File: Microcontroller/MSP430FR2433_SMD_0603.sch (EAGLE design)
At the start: 7 parts, among them IC1 MSP430FR2433IRGET, Y1 32.768kHz

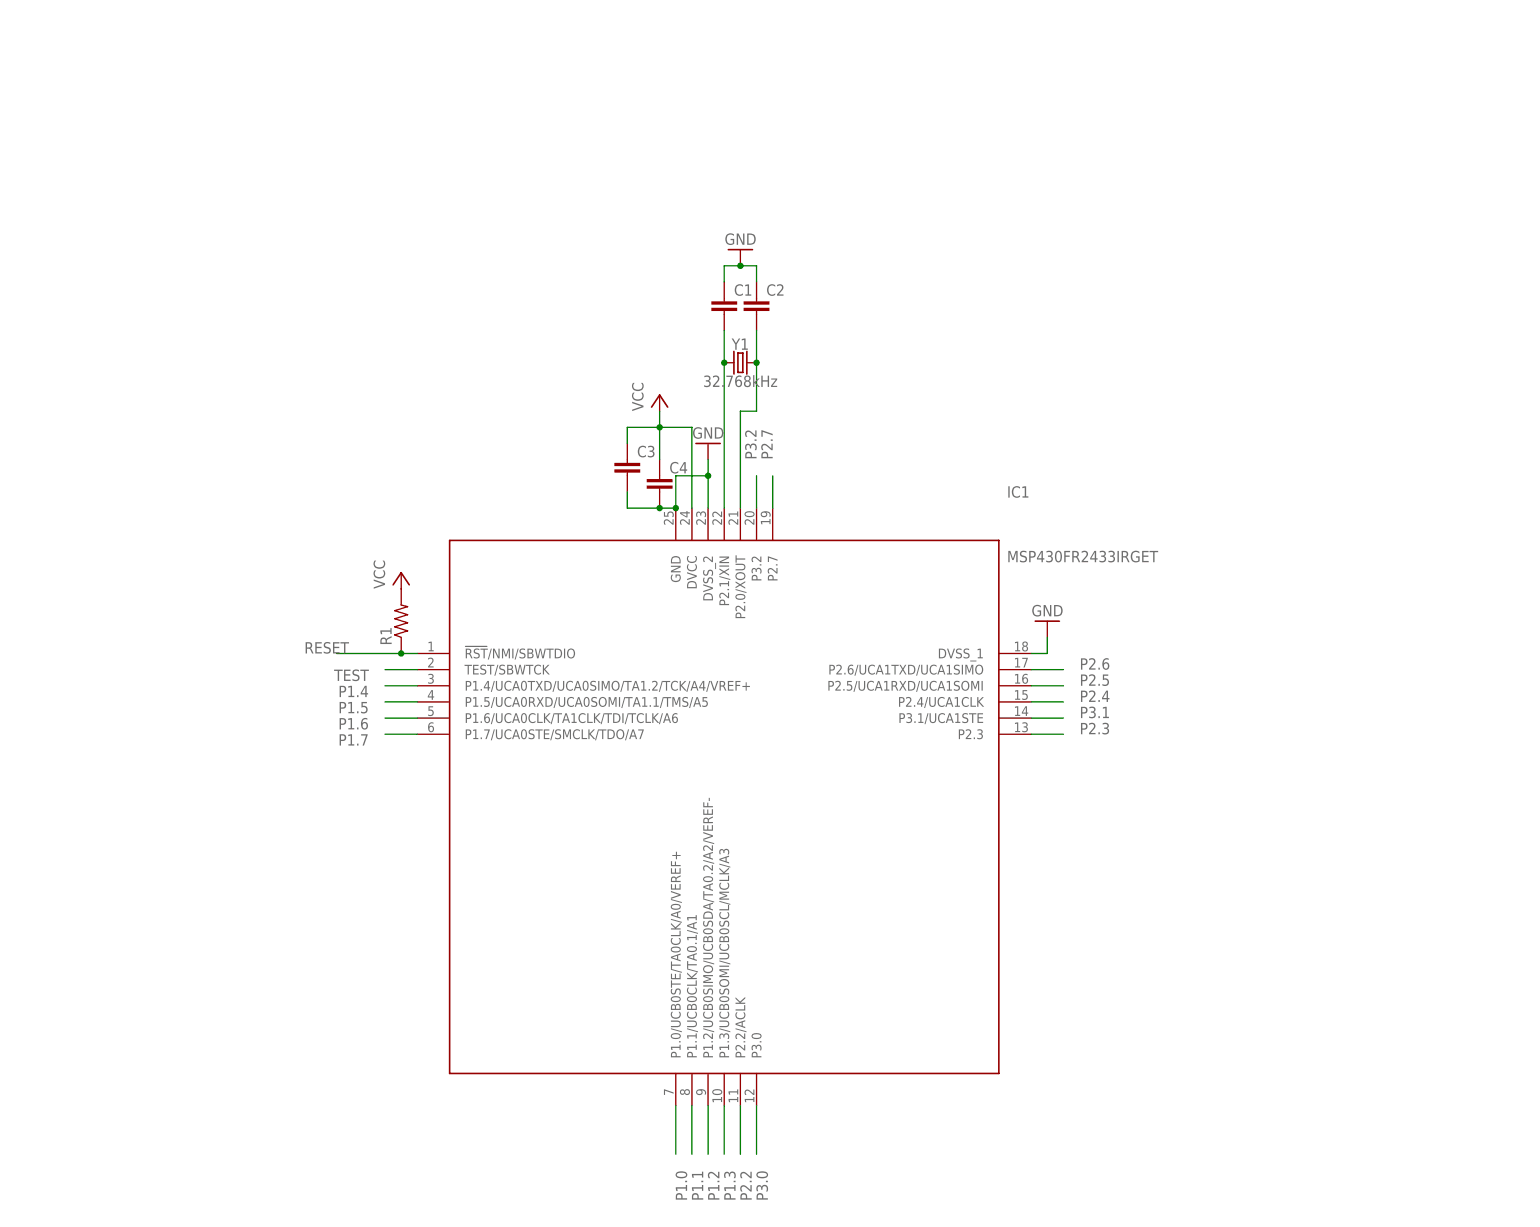
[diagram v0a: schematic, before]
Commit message: msp430fr2433 decice symbol updated
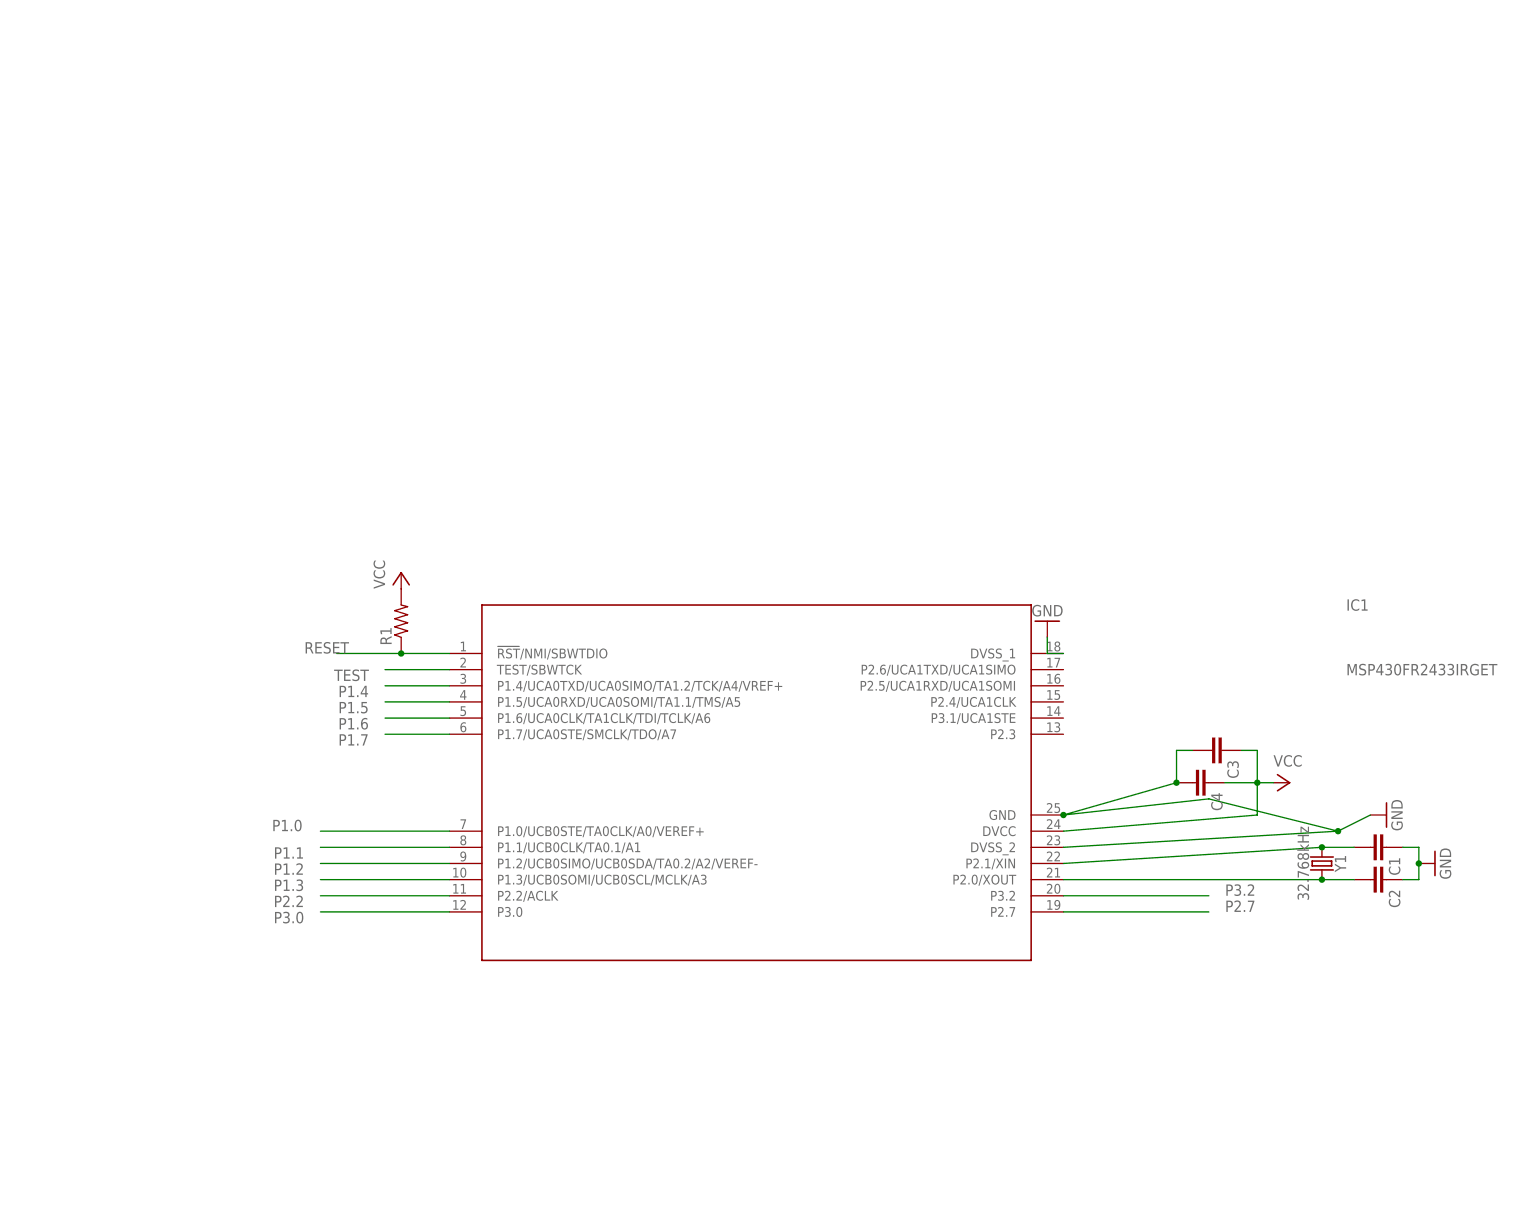
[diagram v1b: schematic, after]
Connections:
- removed net P2.3: IC1.P2.3
- removed net P2.4: IC1.P2.4/UCA1CLK
- removed net P2.5: IC1.P2.5/UCA1RXD/UCA1SOMI
- removed net P2.6: IC1.P2.6/UCA1TXD/UCA1SIMO
- removed net P3.1: IC1.P3.1/UCA1STE
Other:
- moved on the sheet: C1, C2, C3, C4, IC1, Y1

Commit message: msp430fr2433 updated
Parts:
- added IC2: MSP430FR2433IRGET, MSP430fr24333:MSP430FR2433IRGET
- added R2: (no value), rcl:R-US_R0603
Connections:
- new net N$1: IC2.!RST!/NMI/SBWTDIO, R2.1
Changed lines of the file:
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@@
 <?xml version="1.0" encoding="utf-8"?>
 <!DOCTYPE eagle SYSTEM "eagle.dtd">
-<eagle version="9.6.2">
+<eagle version="7.5.0">
 <drawing>
 <settings>
@@
 <parts>
 <part name="IC1" library="SamacSys_Parts" deviceset="MSP430FR2433IRGET" device=""/>
-<part name="R1" library="rcl" library_urn="urn:adsk.eagle:library:334" deviceset="R-US_" device="R0603" package3d_urn="urn:adsk.eagle:package:23555/3"/>
+<part name="R1" library="rcl" deviceset="R-US_" device="R0603"/>
 <part name="Y1" library="SparkFun-Clocks" deviceset="CRYSTAL-32.768KHZ" device="SMD-2X6" value="32.768kHz"/>
-<part name="C1" library="rcl" library_urn="urn:adsk.eagle:library:334" deviceset="C-EU" device="C0603" package3d_urn="urn:adsk.eagle:package:23616/2"/>
-<part name="C2" library="rcl" library_urn="urn:adsk.eagle:library:334" deviceset="C-EU" device="C0603" package3d_urn="urn:adsk.eagle:package:23616/2"/>
+<part name="C1" library="rcl" deviceset="C-EU" device="C0603"/>
+<part name="C2" library="rcl" deviceset="C-EU" device="C0603"/>
 <part name="GND1" library="supply1" deviceset="GND" device=""/>
-<part name="P+1" library="supply1" library_urn="urn:adsk.eagle:library:371" deviceset="VCC" device=""/>
+<part name="P+1" library="supply1@1" deviceset="VCC" device=""/>
 <part name="GND2" library="supply1" deviceset="GND" device=""/>
-<part name="C3" library="rcl" library_urn="urn:adsk.eagle:library:334" deviceset="C-EU" device="C0603" package3d_urn="urn:adsk.eagle:package:23616/2"/>
-<part name="C4" library="rcl" library_urn="urn:adsk.eagle:library:334" deviceset="C-EU" device="C0603" package3d_urn="urn:adsk.eagle:package:23616/2"/>
-<part name="P+2" library="supply1" library_urn="urn:adsk.eagle:library:371" deviceset="VCC" device=""/>
+<part name="C3" library="rcl" deviceset="C-EU" device="C0603"/>
+<part name="C4" library="rcl" deviceset="C-EU" device="C0603"/>
+<part name="P+2" library="supply1@1" deviceset="VCC" device=""/>
 <part name="GND3" library="supply1" deviceset="GND" device=""/>
+<part name="IC2" library="MSP430fr24333" deviceset="MSP430FR2433IRGET" device=""/>
+<part name="R2" library="rcl" deviceset="R-US_" device="R0603"/>
 </parts>
 <sheets>
@@
 <attribute name="VALUE" x="134.62" y="83.82" size="1.778" layer="96" rot="R90"/>
 </instance>
-<instance part="GND3" gate="1" x="238.76" y="78.74" smashed="yes" rot="R180">
-<attribute name="VALUE" x="241.3" y="81.28" size="1.778" layer="96" rot="R180"/>
+<instance part="GND3" gate="1" x="256.54" y="73.66" smashed="yes" rot="R90">
+<attribute name="VALUE" x="259.08" y="71.12" size="1.778" layer="96" rot="R90"/>
+</instance>
+<instance part="IC2" gate="G$1" x="198.12" y="116.84"/>
+<instance part="R2" gate="G$1" x="137.16" y="134.62" smashed="yes" rot="R180">
+<attribute name="NAME" x="138.43" y="133.1214" size="1.778" layer="95" rot="R180"/>
+<attribute name="VALUE" x="140.97" y="137.922" size="1.778" layer="96" rot="R180"/>
 </instance>
 </instances>
@@
 <wire x1="241.3" y1="73.66" x2="238.76" y2="73.66" width="0.1524" layer="91"/>
 <pinref part="GND3" gate="1" pin="GND"/>
-<wire x1="238.76" y1="73.66" x2="238.76" y2="76.2" width="0.1524" layer="91"/>
+<wire x1="241.3" y1="73.66" x2="254" y2="73.66" width="0.1524" layer="91"/>
 </segment>
 </net>
@@
 </segment>
 </net>
+<net name="N$1" class="0">
+<segment>
+<pinref part="R2" gate="G$1" pin="1"/>
+<pinref part="IC2" gate="G$1" pin="!RST!/NMI/SBWTDIO"/>
+<wire x1="142.24" y1="134.62" x2="149.86" y2="134.62" width="0.1524" layer="91"/>
+</segment>
+</net>
 </nets>
 </sheet>
@@
 </schematic>
 </drawing>
-<compatibility>
-<note version="8.2" severity="warning">
-Since Version 8.2, EAGLE supports online libraries. The ids
-of those online libraries will not be understood (or retained)
-with this version.
-</note>
-<note version="8.3" severity="warning">
-Since Version 8.3, EAGLE supports URNs for individual library
-assets (packages, symbols, and devices). The URNs of those assets
-will not be understood (or retained) with this version.
-</note>
-<note version="8.3" severity="warning">
-Since Version 8.3, EAGLE supports the association of 3D packages
-with devices in libraries, schematics, and board files. Those 3D
-packages will not be understood (or retained) with this version.
-</note>
-<note version="8.4" severity="warning">
-Since Version 8.4, EAGLE supports properties for SPICE simulation.
-Probes in schematics and SPICE mapping objects found in parts and library devices
-will not be understood with this version. Update EAGLE to the latest version
-for full support of SPICE simulation.
-</note>
-</compatibility>
 </eagle>

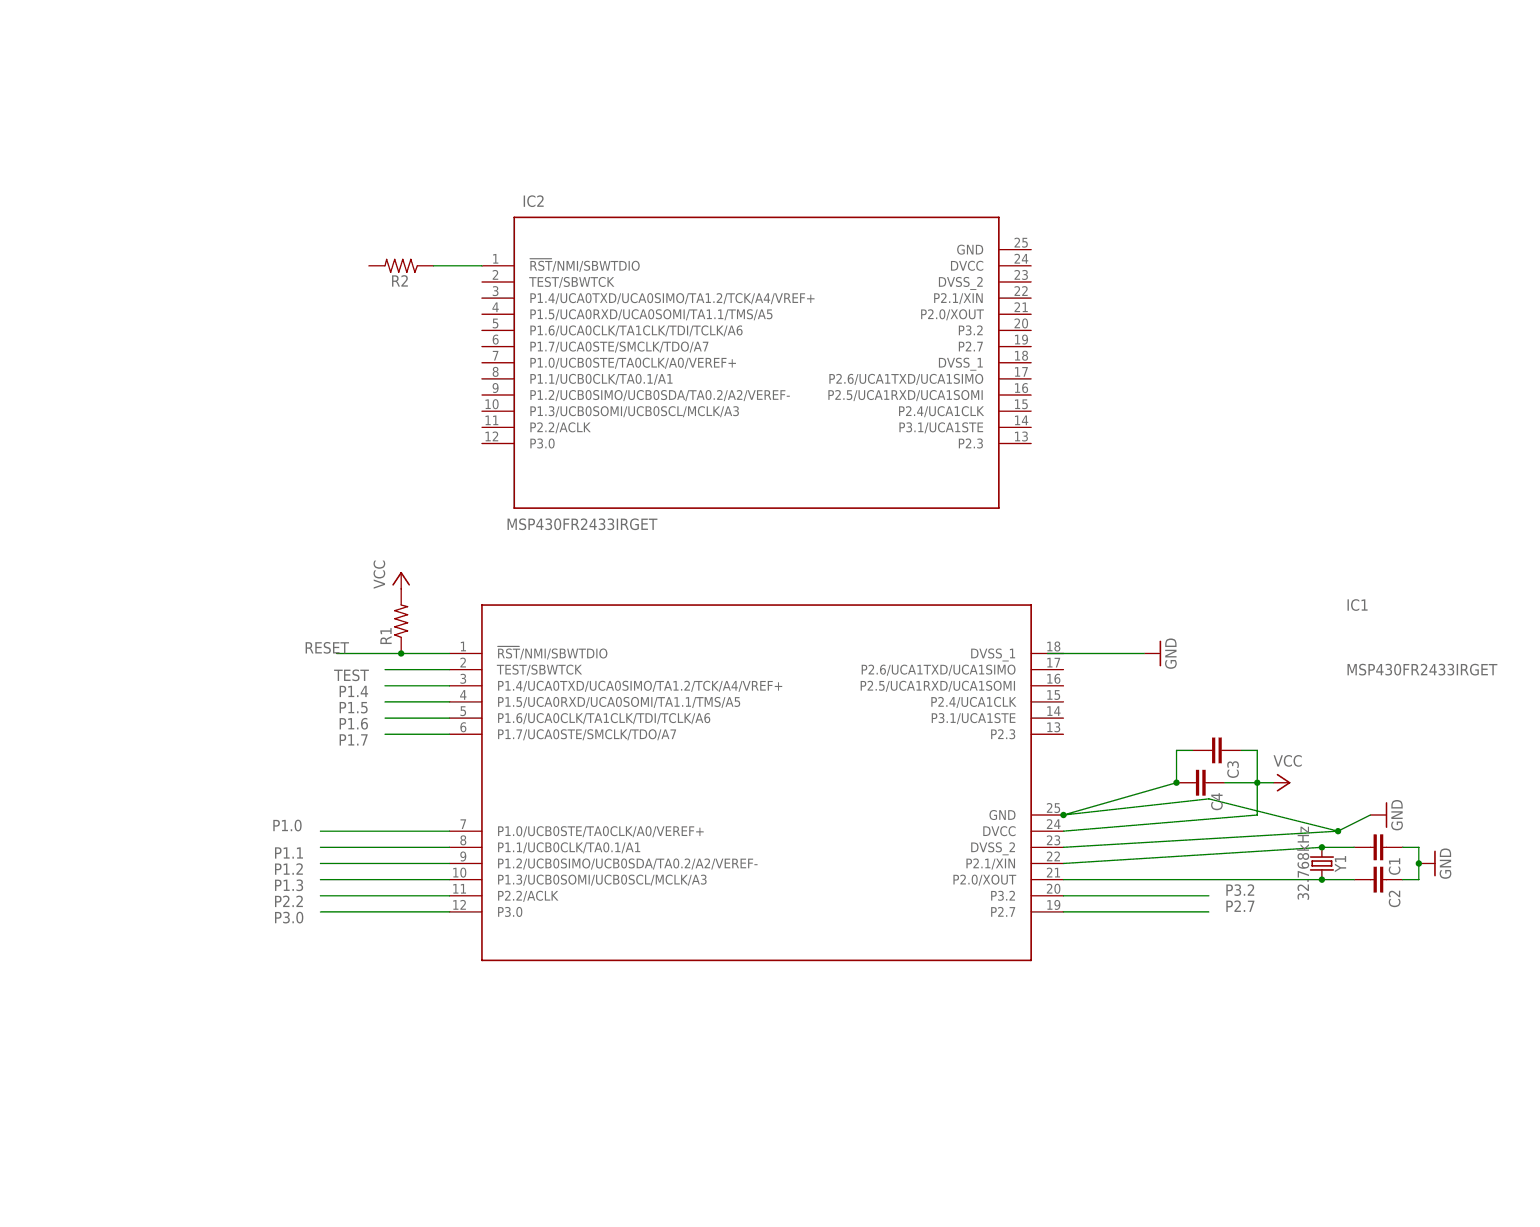
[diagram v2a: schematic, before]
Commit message: msp430fr2433 added
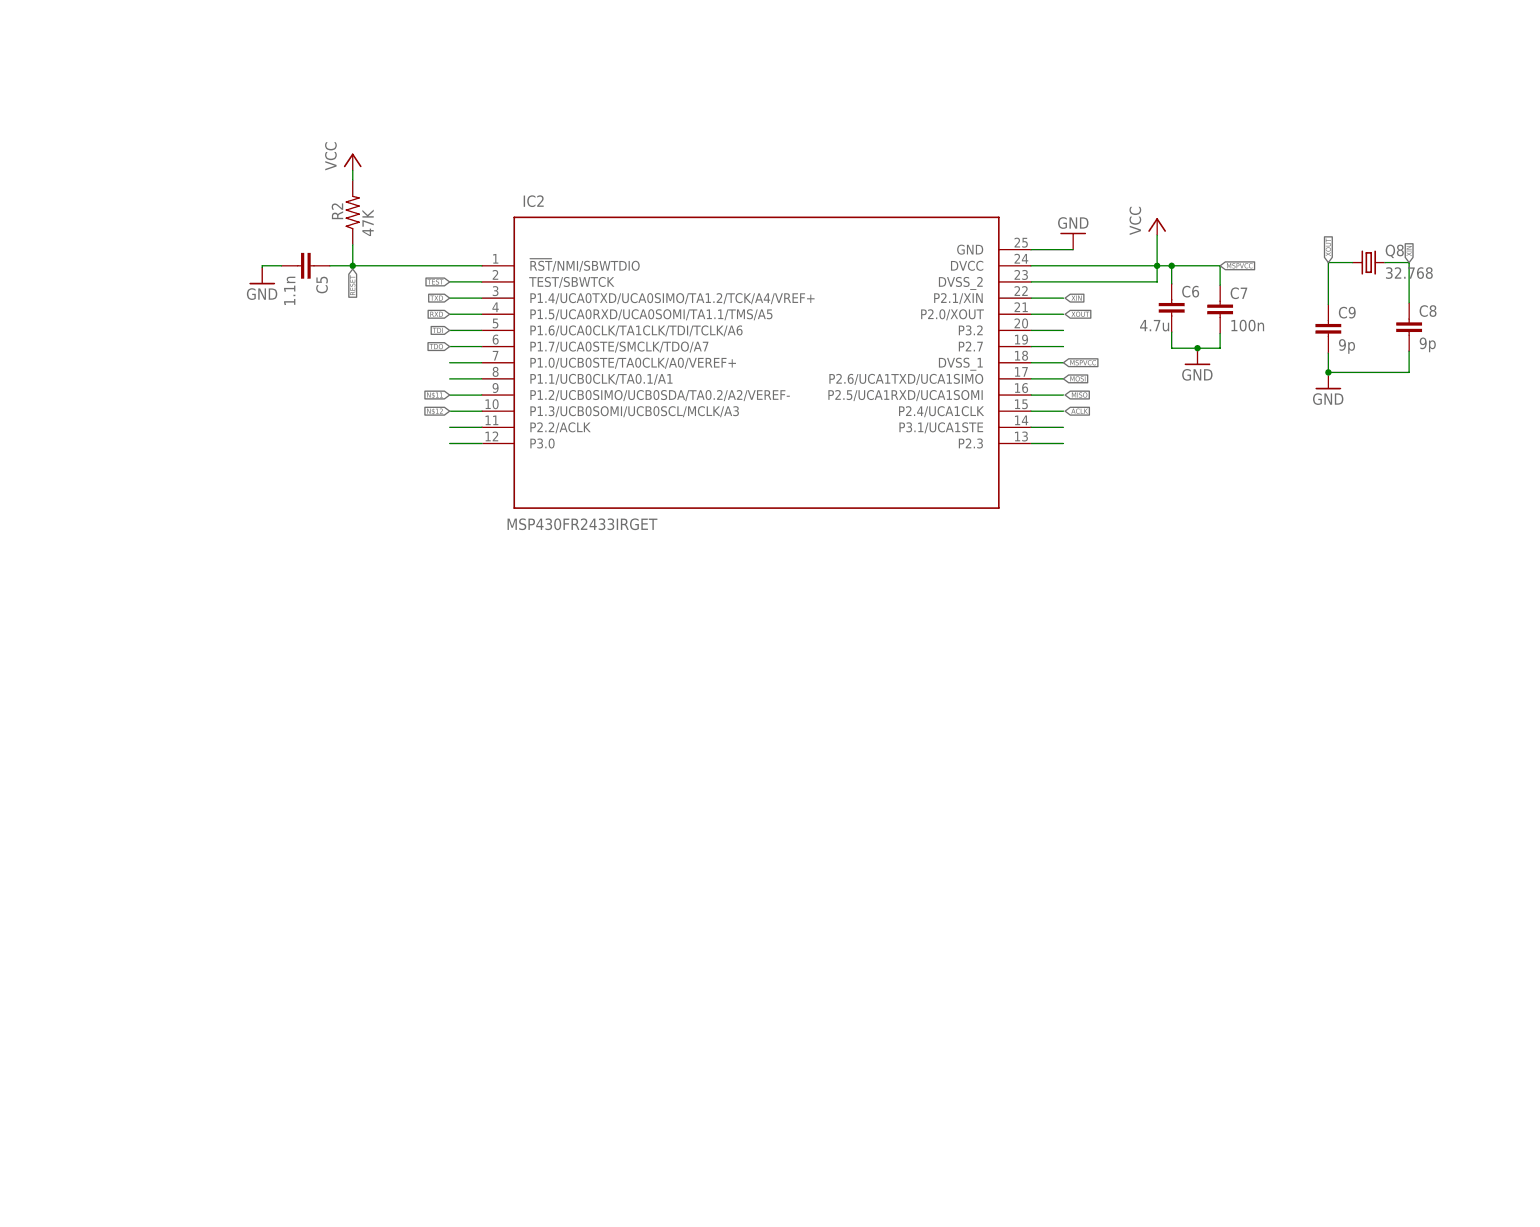
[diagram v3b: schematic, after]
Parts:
- removed C1, C2, C3, C4: (no value), rcl:C-EUC0603
- removed IC1: MSP430FR2433IRGET, SamacSys_Parts:MSP430FR2433IRGET
- removed R1: (no value), rcl:R-US_R0603
- removed Y1: 32.768kHz, SparkFun-Clocks:CRYSTAL-32.768KHZSMD-2X6
- added C5: 1.1n, rcl:C-EUC0402
- added C6: 4.7u, rcl:C-EUC0402
- added C7: 100n, rcl:C-EUC0402
- added C8, C9: 9p, rcl:C-EUC0402
- added Q8: 32.768, crystal:CRYTALTC26H
- R2: value (none) -> 47K; device rcl:R-US_R0603 -> rcl:R-US_R0402
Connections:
- removed net N$1: IC2.!RST!/NMI/SBWTDIO, R2.1
- removed net N$5: C1.2, IC1.P2.1/XIN, Y1.1
- removed net N$6: C2.2, IC1.P2.0/XOUT, Y1.2
- removed net P1.0: IC1.P1.0/UCB0STE/TA0CLK/A0/VEREF+
- removed net P1.1: IC1.P1.1/UCB0CLK/TA0.1/A1
- removed net P1.2: IC1.P1.2/UCB0SIMO/UCB0SDA/TA0.2/A2/VEREF-
- removed net P1.3: IC1.P1.3/UCB0SOMI/UCB0SCL/MCLK/A3
- removed net P1.4: IC1.P1.4/UCA0TXD/UCA0SIMO/TA1.2/TCK/A4/VREF+
- removed net P1.5: IC1.P1.5/UCA0RXD/UCA0SOMI/TA1.1/TMS/A5
- removed net P1.6: IC1.P1.6/UCA0CLK/TA1CLK/TDI/TCLK/A6
- removed net P1.7: IC1.P1.7/UCA0STE/SMCLK/TDO/A7
- removed net P2.2: IC1.P2.2/ACLK
- removed net P2.7: IC1.P2.7
- removed net P3.0: IC1.P3.0
- removed net P3.2: IC1.P3.2
- new net ACLK: IC2.P2.4/UCA1CLK
- new net MISO: IC2.P2.5/UCA1RXD/UCA1SOMI
- new net MOSI: IC2.P2.6/UCA1TXD/UCA1SIMO
- new net MSPVCC: C6.1, C7.1, IC2.DVCC, IC2.DVSS_1, IC2.DVSS_2
- new net N$10: IC2.P1.1/UCB0CLK/TA0.1/A1
- new net N$11: IC2.P1.2/UCB0SIMO/UCB0SDA/TA0.2/A2/VEREF-
- new net N$12: IC2.P1.3/UCB0SOMI/UCB0SCL/MCLK/A3
- new net N$13: IC2.P2.2/ACLK
- new net N$14: IC2.P3.0
- new net N$20: IC2.P3.2
- new net N$21: IC2.P2.7
- new net N$26: IC2.P3.1/UCA1STE
- new net N$27: IC2.P2.3
- new net N$9: IC2.P1.0/UCB0STE/TA0CLK/A0/VEREF+
- new net RXD: IC2.P1.5/UCA0RXD/UCA0SOMI/TA1.1/TMS/A5
- new net TDI: IC2.P1.6/UCA0CLK/TA1CLK/TDI/TCLK/A6
- new net TDO: IC2.P1.7/UCA0STE/SMCLK/TDO/A7
- new net TXD: IC2.P1.4/UCA0TXD/UCA0SIMO/TA1.2/TCK/A4/VREF+
- new net XIN: C8.1, IC2.P2.1/XIN, Q8.2
- new net XOUT: C9.1, IC2.P2.0/XOUT, Q8.1
- net GND: now also C5.2, C6.2, C7.2, C8.2, C9.2, IC2.GND; no longer C1.1, C2.1, C3.2, C4.2, IC1.DVSS_1, IC1.DVSS_2, IC1.GND
- net RESET: now also C5.1, IC2.!RST!/NMI/SBWTDIO, R2.1; no longer IC1.!RST!/NMI/SBWTDIO, R1.1
- net TEST: now also IC2.TEST/SBWTCK; no longer IC1.TEST/SBWTCK
- net VCC: now also R2.2; no longer C3.1, C4.1, IC1.DVCC, R1.2
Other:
- moved on the sheet: R2
